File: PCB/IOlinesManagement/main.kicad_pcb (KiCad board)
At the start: 2 copper layers, 177.8 x 104 mm, 286 parts, among them K1 HK19F-DCxxV-SHC, K10 HK19F-DCxxV-SHC, K11 HK19F-DCxxV-SHC, K12 HK19F-DCxxV-SHC, K13 HK19F-DCxxV-SHC, K14 HK19F-DCxxV-SHC, K15 HK19F-DCxxV-SHC, K16 HK19F-DCxxV-SHC, K2 HK19F-DCxxV-SHC, K3 HK19F-DCxxV-SHC, K4 HK19F-DCxxV-SHC, K5 HK19F-DCxxV-SHC, K6 HK19F-DCxxV-SHC, K7 HK19F-DCxxV-SHC, K8 HK19F-DCxxV-SHC, K9 HK19F-DCxxV-SHC, Q1 BC817, Q10 BC817, Q11 BC817, Q12 BC817, Q13 BC817, Q14 BC817, Q15 BC817, Q16 BC817, Q17 BC817, Q18 BC817, Q19 BC817, Q2 BC817, Q20 BC817, Q21 BC817, Q22 BC817, Q23 BC337, Q24 BC337, Q25 BC337, Q26 BC337, Q27 BC337, Q28 BC337, Q29 BC337, Q3 BC817, Q30 BC337, Q31 BC337, Q32 BC337, Q33 BC337, Q34 BC337, Q35 BC327, Q36 BC337, Q37 BC337, Q38 BC337, Q39 BC337, Q4 BC817, Q40 BC337, Q41 BC337, Q42 BC337, Q43 BC337, Q44 BC337, Q45 BC337, Q46 BC337, Q47 BC337, Q48 BC337, Q49 BC337, Q5 BC817, Q50 BC337, Q51 BC327, Q52 BC337, Q53 BC337, Q54 BC337, Q55 BC337, Q56 BC337, Q57 BC337, Q58 BC337, Q59 BC337, Q6 BC817, Q60 BC337, Q61 BC337, Q62 BC337, Q63 BC337, Q64 BC337, Q65 BC337, Q66 BC337, Q67 BC327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

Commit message: 99% completed release
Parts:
- removed ExtPwr_1: Conn_01x02, Connector_PinHeader_2.54mm:PinHeader_2x09_P2.54mm_Vertical
- removed Q65, Q66: BC337, Package_TO_SOT_THT:TO-92_Inline_Wide
- removed Q67, Q68, Q69, Q70, Q71, Q72, Q73, Q74, Q75, Q76, Q77, Q78, Q79, Q80: BC327, Package_TO_SOT_THT:TO-92_Inline_Wide
- removed Q81, Q82, Q83, Q84, Q85, Q86, Q87, Q88, Q89, Q90: BC817, Package_TO_SOT_SMD:SOT-23
- Q17, Q19, Q21: value BC817 -> BC327; footprint Package_TO_SOT_SMD:SOT-23 -> Package_TO_SOT_THT:TO-92_Inline_Wide
- Q18, Q20, Q22: value BC817 -> BC337; footprint Package_TO_SOT_SMD:SOT-23 -> Package_TO_SOT_THT:TO-92_Inline_Wide
- Q23, Q25, Q26, Q28, Q30, Q32, Q34, Q37, Q39, Q41, Q43, Q45, Q47, Q49, Q52, Q53, Q54, Q55, Q56, Q57, Q58, Q59, Q60, Q61, Q62, Q63, Q64: value BC337 -> BC327
- R100, R101, R104, R29, R32, R42, R45, R46, R73, R74, R97: value 100 -> 50
- R102, R103, R23, R26, R35, R43, R44, R59, R68, R71, R72, R75, R91, R94: value 100 -> 5K
- R17, R18, R19, R20, R55, R83: value 10K -> 100K
- R21, R50, R53, R81: value 10K -> 50
- R22, R47, R51, R52, R76, R79, R80: value 10K -> 5K
- R24, R25, R28, R33, R36, R57, R60, R66, R69, R70, R89, R92, R93, R96: value 5K -> 50
- R37, R39, R61, R63, R64, R86, R87: value 5K -> 100K
- R38, R41, R62, R85, R88: value 100 -> 100K
- R40: value 5K -> 10K
- R48: value 1K -> 5K
- R49, R78: value 100K -> 50
- R54, R82: value 10K -> 1K
- R56, R65: value 100 -> 10K
- R77: value 1K -> 50
- moved Q45 339.7 mm to (188.7, 142.8)
- moved Q37 335.9 mm to (188.7, 120.3)
- moved Q29 332.8 mm to (184.3, 81.0)
- moved Q19 331.0 mm to (187.8, 74.8)
- moved Q46 324.3 mm to (183.9, 127.4)
- moved Q63 321.0 mm to (177.1, 126.6), turned to 180 degrees
- moved Q20 318.9 mm to (184.2, 59.2)
- moved Q38 310.1 mm to (183.9, 104.7)
- moved Q26 306.6 mm to (158.2, 96.6)
- moved Q64 304.6 mm to (177.1, 104.1), turned to 180 degrees
- moved R70 303.9 mm to (193.6, 115.1), turned to 90 degrees
- moved Q36 303.0 mm to (154.2, 104.9)
- moved Q18 301.6 mm to (153.8, 58.8)
- moved R93 301.2 mm to (193.6, 137.7), turned to 90 degrees
- moved R86 298.8 mm to (179.3, 127.1), turned to -90 degrees
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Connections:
- K10 pad A1: Net-(Q10-C) -> Net-(Q11-C)
- K11 pad A1: Net-(Q11-C) -> Net-(Q12-C)
- K12 pad A1: Net-(Q12-C) -> Net-(Q9-C)
- K13 pad A1: Net-(Q16-C) -> Net-(Q14-C)
- K14 pad A1: Net-(Q15-C) -> Net-(Q13-C)
- K15 pad A1: Net-(Q14-C) -> Net-(Q15-C)
- K16 pad A1: Net-(Q13-C) -> Net-(Q16-C)
- K5 pad A1: Net-(Q5-C) -> Net-(Q7-C)
- K7 pad A1: Net-(Q7-C) -> Net-(Q8-C)
- K8 pad A1: Net-(Q8-C) -> Net-(Q5-C)
- K9 pad A1: Net-(Q9-C) -> Net-(Q10-C)
- Q17 pad 1: Net-(Q17-B) -> OutputToDev_9
- Q17 pad 2: GND -> Net-(Q17-B)
- Q17 pad 3: Net-(Q17-C) -> Net-(Q17-E)
- Q18 pad 1: Net-(Q18-B) -> OutputToDev_9
- Q18 pad 2: GND -> Net-(Q18-B)
- Q18 pad 3: Net-(Q18-C) -> Net-(Q18-E)
- Q19 pad 1: Net-(Q19-B) -> OutputToDev_13
- Q19 pad 2: GND -> Net-(Q19-B)
- Q19 pad 3: Net-(Q19-C) -> Net-(Q19-E)
- Q20 pad 1: Net-(Q20-B) -> OutputToDev_13
- Q20 pad 2: GND -> Net-(Q20-B)
- Q20 pad 3: Net-(Q20-C) -> Net-(Q20-E)
- Q21 pad 1: Net-(Q21-B) -> OutputToDev_1
- Q21 pad 2: GND -> Net-(Q21-B)
- Q21 pad 3: Net-(Q21-C) -> Net-(Q21-E)
- Q22 pad 1: Net-(Q22-B) -> OutputToDev_1
- Q22 pad 2: GND -> Net-(Q22-B)
- Q22 pad 3: Net-(Q22-C) -> Net-(Q22-E)
- Q23 pad 1: Net-(Q23-C) -> OutputToDev_5
- Q23 pad 3: OutputToDev_1 -> Net-(Q23-E)
- Q24 pad 1: Net-(Q24-C) -> OutputToDev_5
- Q24 pad 2: Net-(Q17-C) -> Net-(Q24-B)
- Q24 pad 3: GND -> Net-(Q24-E)
- Q25 pad 1: Net-(Q25-C) -> InputToMC_1
- Q25 pad 3: OutputToDev_4 -> Net-(Q25-E)
- Q26 pad 1: Net-(Q26-C) -> OutputToDev_10
- Q26 pad 3: GND -> Net-(Q26-E)
- Q27 pad 1: Net-(Q27-C) -> OutputToDev_10
- Q27 pad 3: OutputToDev_7 -> Net-(Q27-E)
- Q28 pad 1: Net-(Q28-C) -> OutputToDev_14
- Q28 pad 2: Net-(Q18-C) -> Net-(Q28-B)
- Q28 pad 3: GND -> Net-(Q28-E)
- Q29 pad 1: Net-(Q29-C) -> OutputToDev_14
- Q29 pad 3: OutputToDev_13 -> Net-(Q29-E)
- Q30 pad 1: Net-(Q30-C) -> OutputToDev_2
- Q30 pad 3: GND -> Net-(Q30-E)
- Q31 pad 1: Net-(Q31-C) -> OutputToDev_2
- Q31 pad 3: OutputToDev_10 -> Net-(Q31-E)
- Q32 pad 1: Net-(Q32-C) -> OutputToDev_6
- Q32 pad 2: Net-(Q19-C) -> Net-(Q32-B)
- Q32 pad 3: GND -> Net-(Q32-E)
- Q33 pad 1: Net-(Q33-C) -> OutputToDev_6
- Q33 pad 3: OutputToDev_16 -> Net-(Q33-E)
- Q34 pad 1: Net-(Q34-C) -> InputToMC_2
- Q34 pad 3: GND -> Net-(Q34-E)
- Q35 pad 1: InputToMC_1 -> OutputToDev_11
- Q36 pad 1: Net-(Q36-C) -> OutputToDev_11
- Q36 pad 3: GND -> Net-(Q36-E)
- Q37 pad 1: Net-(Q37-C) -> OutputToDev_15
- Q37 pad 3: GND -> Net-(Q37-E)
- Q38 pad 1: Net-(Q38-C) -> OutputToDev_15
- Q38 pad 3: GND -> Net-(Q38-E)
- Q39 pad 1: Net-(Q39-C) -> OutputToDev_3
- Q39 pad 3: unconnected-(Q39-E-Pad3) -> Net-(Q39-E)
- Q40 pad 1: Net-(Q40-C) -> OutputToDev_3
- Q40 pad 3: GND -> Net-(Q40-E)
- Q41 pad 1: Net-(Q41-C) -> OutputToDev_7
- Q41 pad 3: OutputToDev_2 -> Net-(Q41-E)
- Q42 pad 1: Net-(Q42-C) -> OutputToDev_7
- Q42 pad 3: GND -> Net-(Q42-E)
- Q43 pad 1: Net-(Q43-C) -> OutputToDev_12
- Q43 pad 3: OutputToDev_5 -> Net-(Q43-E)
- Q44 pad 1: Net-(Q44-C) -> OutputToDev_12
- Q44 pad 3: GND -> Net-(Q44-E)
- Q45 pad 1: Net-(Q45-C) -> OutputToDev_16
- Q45 pad 3: OutputToDev_8 -> Net-(Q45-E)
- Q46 pad 1: Net-(Q46-C) -> OutputToDev_16
- Q46 pad 2: Net-(Q22-C) -> Net-(Q46-B)
- Q46 pad 3: GND -> Net-(Q46-E)
- Q47 pad 1: Net-(Q47-C) -> OutputToDev_4
- Q47 pad 3: OutputToDev_14 -> Net-(Q47-E)
- Q48 pad 1: Net-(Q48-C) -> OutputToDev_4
- Q48 pad 2: Net-(Q20-C) -> Net-(Q48-B)
- Q48 pad 3: GND -> Net-(Q48-E)
- Q49 pad 1: Net-(Q49-C) -> OutputToDev_8
- Q49 pad 3: OutputToDev_11 -> Net-(Q49-E)
- Q50 pad 1: Net-(Q50-C) -> OutputToDev_8
- Q50 pad 2: Net-(Q21-C) -> Net-(Q50-B)
- Q50 pad 3: GND -> Net-(Q50-E)
- Q51 pad 1: InputToMC_2 -> InputToMC_8
- Q52 pad 1: Net-(Q52-C) -> InputToMC_10
- Q52 pad 3: GND -> Net-(Q52-E)
- Q53 pad 1: Net-(Q53-C) -> InputToMC_5
- Q53 pad 3: GND -> Net-(Q53-E)
- Q54 pad 1: Net-(Q54-C) -> InputToMC_9
- Q54 pad 3: GND -> Net-(Q54-E)
- Q55 pad 1: Net-(Q55-C) -> InputToMC_12
- Q55 pad 3: GND -> Net-(Q55-E)
- Q56 pad 1: Net-(Q56-C) -> InputToMC_11
- Q56 pad 3: GND -> Net-(Q56-E)
- Q57 pad 1: Net-(Q57-C) -> InputToMC_4
- Q57 pad 3: OutputToDev_3 -> Net-(Q57-E)
- Q58 pad 1: Net-(Q58-C) -> InputToMC_3
- Q58 pad 3: GND -> Net-(Q58-E)
- Q59 pad 1: Net-(Q59-C) -> InputToMC_6
- Q59 pad 3: OutputToDev_6 -> Net-(Q59-E)
- Q60 pad 1: Net-(Q60-C) -> InputToMC_14
- Q60 pad 3: GND -> Net-(Q60-E)
- Q61 pad 1: Net-(Q61-C) -> InputToMC_7
- Q61 pad 3: OutputToDev_9 -> Net-(Q61-E)
- Q62 pad 1: Net-(Q62-C) -> InputToMC_13
- Q62 pad 3: GND -> Net-(Q62-E)
- Q63 pad 1: Net-(Q63-C) -> InputToMC_16
- Q63 pad 3: OutputToDev_15 -> Net-(Q63-E)
- Q64 pad 1: Net-(Q64-C) -> InputToMC_15
- Q64 pad 3: GND -> Net-(Q64-E)
- R10 pad 1: Net-(Q10-B) -> Net-(Q11-B)
- R100 pad 1: OutputToDev_3 -> Net-(Q48-E)
- R100 pad 2: Net-(Q58-C) -> GND
- R101 pad 1: OutputToDev_6 -> Net-(Q49-E)
- R101 pad 2: Net-(Q60-C) -> +5V
- R102 pad 1: OutputToDev_9 -> OutputToMC_8
- R102 pad 2: Net-(Q62-C) -> Net-(Q49-B)
- R103 pad 1: OutputToDev_15 -> OutputToMC_8
- R103 pad 2: Net-(Q64-C) -> Net-(Q50-B)
- R104 pad 1: OutputToDev_12 -> Net-(Q50-E)
- R104 pad 2: Net-(Q66-C) -> GND
- R11 pad 1: Net-(Q9-B) -> Net-(Q10-B)
- R112 pad 1: Net-(Q67-E) -> Net-(Q51-E)
- R113 pad 1: Net-(Q68-E) -> Net-(Q52-E)
- R114 pad 1: Net-(Q69-E) -> Net-(Q53-E)
- R115 pad 1: Net-(Q67-B) -> Net-(Q51-B)
- R116 pad 2: Net-(Q67-B) -> Net-(Q51-B)
- R117 pad 1: Net-(Q70-E) -> Net-(Q54-E)
- R118 pad 1: Net-(Q68-B) -> Net-(Q52-B)
- R119 pad 2: Net-(Q68-B) -> Net-(Q52-B)
- R12 pad 1: Net-(Q11-B) -> Net-(Q12-B)
- R120 pad 1: Net-(Q71-E) -> Net-(Q55-E)
- R121 pad 1: Net-(Q69-B) -> Net-(Q53-B)
- R122 pad 2: Net-(Q69-B) -> Net-(Q53-B)
- R123 pad 1: Net-(Q70-B) -> Net-(Q54-B)
- R124 pad 2: Net-(Q70-B) -> Net-(Q54-B)
- R125 pad 1: Net-(Q72-E) -> Net-(Q56-E)
- R126 pad 1: Net-(Q71-B) -> Net-(Q55-B)
- R127 pad 2: Net-(Q71-B) -> Net-(Q55-B)
- R128 pad 1: Net-(Q73-E) -> Net-(Q57-E)
- R129 pad 1: Net-(Q72-B) -> Net-(Q56-B)
- R13 pad 1: Net-(Q16-B) -> Net-(Q14-B)
- R130 pad 2: Net-(Q72-B) -> Net-(Q56-B)
- R131 pad 1: Net-(Q73-B) -> Net-(Q57-B)
- R132 pad 2: Net-(Q73-B) -> Net-(Q57-B)
- R14 pad 1: Net-(Q14-B) -> Net-(Q15-B)
- R140 pad 1: Net-(Q74-E) -> Net-(Q58-E)
- R141 pad 1: Net-(Q74-B) -> Net-(Q58-B)
- R142 pad 2: Net-(Q74-B) -> Net-(Q58-B)
- R143 pad 1: Net-(Q75-E) -> Net-(Q59-E)
- R144 pad 1: Net-(Q75-B) -> Net-(Q59-B)
- R145 pad 2: Net-(Q75-B) -> Net-(Q59-B)
- R146 pad 1: Net-(Q76-E) -> Net-(Q60-E)
- R147 pad 1: Net-(Q77-E) -> Net-(Q61-E)
- R148 pad 1: Net-(Q78-E) -> Net-(Q62-E)
- R149 pad 1: Net-(Q76-B) -> Net-(Q60-B)
- R15 pad 1: Net-(Q13-B) -> Net-(Q16-B)
- R150 pad 2: Net-(Q76-B) -> Net-(Q60-B)
- R151 pad 1: Net-(Q79-E) -> Net-(Q63-E)
- R152 pad 1: Net-(Q77-B) -> Net-(Q61-B)
- R153 pad 2: Net-(Q77-B) -> Net-(Q61-B)
- R154 pad 1: Net-(Q78-B) -> Net-(Q62-B)
- R155 pad 2: Net-(Q78-B) -> Net-(Q62-B)
- R156 pad 1: Net-(Q80-E) -> Net-(Q64-E)
- R157 pad 1: Net-(Q79-B) -> Net-(Q63-B)
- R158 pad 2: Net-(Q79-B) -> Net-(Q63-B)
- R159 pad 1: Net-(Q80-B) -> Net-(Q64-B)
- R16 pad 1: Net-(Q15-B) -> Net-(Q13-B)
- R160 pad 2: Net-(Q80-B) -> Net-(Q64-B)
- R17 pad 1: OutputToMC_1 -> GND
- R17 pad 2: Net-(Q17-B) -> OutputToDev_9
- R18 pad 1: OutputToMC_4 -> GND
- R18 pad 2: Net-(Q81-B) -> OutputToDev_13
- R19 pad 1: OutputToMC_7 -> GND
- R19 pad 2: Net-(Q18-B) -> OutputToDev_1
- R20 pad 1: OutputToMC_13 -> GND
- R20 pad 2: Net-(Q82-B) -> OutputToDev_5
- R21 pad 1: OutputToMC_10 -> Net-(Q17-E)
- R21 pad 2: Net-(Q19-B) -> +5V
- R22 pad 1: OutputToMC_16 -> OutputToMC_9
- R22 pad 2: Net-(Q83-B) -> Net-(Q17-B)
- R23 pad 1: VCC -> OutputToMC_9
- R23 pad 2: Net-(Q23-C) -> Net-(Q18-B)
- R24 pad 1: Net-(Q23-B) -> Net-(Q18-E)
- R24 pad 2: OutputToMC_1 -> GND
- R25 pad 1: +5V -> Net-(Q19-E)
- R25 pad 2: Net-(Q17-C) -> +5V
- R26 pad 1: VCC -> OutputToMC_13
- R26 pad 2: Net-(Q25-C) -> Net-(Q19-B)
- R27 pad 1: Net-(Q25-B) -> OutputToMC_13
- R27 pad 2: OutputToMC_4 -> Net-(Q20-B)
- R28 pad 1: +5V -> Net-(Q21-E)
- R28 pad 2: Net-(Q26-B) -> +5V
- R29 pad 1: VCC -> Net-(Q20-E)
- R29 pad 2: Net-(Q27-C) -> GND
- R30 pad 1: Net-(Q27-B) -> OutputToMC_1
- R30 pad 2: OutputToMC_7 -> Net-(Q21-B)
- R31 pad 1: +5V -> OutputToMC_1
- R31 pad 2: Net-(Q18-C) -> Net-(Q22-B)
- R32 pad 1: VCC -> Net-(Q22-E)
- R32 pad 2: Net-(Q29-C) -> GND
- R33 pad 1: Net-(Q29-B) -> Net-(Q23-E)
- R33 pad 2: OutputToMC_13 -> +5V
- R34 pad 1: +5V -> OutputToMC_5
- R34 pad 2: Net-(Q30-B) -> Net-(Q23-B)
- R35 pad 1: VCC -> OutputToMC_5
- R35 pad 2: Net-(Q31-C) -> Net-(Q24-B)
- R36 pad 1: Net-(Q31-B) -> Net-(Q24-E)
- R36 pad 2: OutputToMC_10 -> GND
- R37 pad 1: +5V -> GND
- R37 pad 2: Net-(Q19-C) -> OutputToDev_10
- R38 pad 1: VCC -> GND
- R38 pad 2: Net-(Q33-C) -> OutputToDev_14
- R39 pad 1: Net-(Q33-B) -> GND
- R39 pad 2: OutputToMC_16 -> OutputToDev_2
- R40 pad 1: +5V -> InputToMC_1
- R40 pad 2: Net-(Q34-B) -> GND
- R41 pad 1: OutputToDev_1 -> GND
- R41 pad 2: Net-(Q24-C) -> OutputToDev_6
- R42 pad 1: OutputToDev_4 -> Net-(Q26-E)
- R42 pad 2: Net-(Q26-C) -> +5V
- R43 pad 1: OutputToDev_7 -> OutputToMC_10
- R43 pad 2: Net-(Q28-C) -> Net-(Q26-B)
- R44 pad 1: OutputToDev_13 -> OutputToMC_10
- R44 pad 2: Net-(Q30-C) -> Net-(Q27-B)
- R45 pad 1: OutputToDev_10 -> Net-(Q27-E)
- R45 pad 2: Net-(Q32-C) -> GND
- R46 pad 1: OutputToDev_16 -> Net-(Q28-E)
- R46 pad 2: Net-(Q34-C) -> +5V
- R47 pad 1: InputToMC_1 -> OutputToMC_14
- R47 pad 2: GND -> Net-(Q28-B)
- R48 pad 1: Net-(Q35-E) -> OutputToMC_14
- R48 pad 2: +5V -> Net-(Q29-B)
- R49 pad 1: Net-(Q35-B) -> Net-(Q30-E)
- R5 pad 1: Net-(Q5-B) -> Net-(Q7-B)
- R50 pad 1: InputToDev_1 -> Net-(Q29-E)
- R50 pad 2: Net-(Q35-B) -> GND
- R51 pad 2: Net-(Q85-B) -> Net-(Q30-B)
- R52 pad 1: OutputToMC_5 -> OutputToMC_2
- R52 pad 2: Net-(Q84-B) -> Net-(Q31-B)
- R53 pad 1: OutputToMC_8 -> Net-(Q31-E)
- R53 pad 2: Net-(Q22-B) -> GND
- R54 pad 1: OutputToMC_14 -> Net-(Q25-E)
- R54 pad 2: Net-(Q20-B) -> +5V
- R55 pad 1: OutputToMC_11 -> Net-(Q25-B)
- R55 pad 2: Net-(Q21-B) -> +5V
- R56 pad 1: VCC -> InputToDev_1
- R56 pad 2: Net-(Q41-C) -> Net-(Q25-B)
- R57 pad 1: Net-(Q41-B) -> Net-(Q32-E)
- R57 pad 2: OutputToMC_2 -> +5V
- R58 pad 1: +5V -> OutputToMC_6
- R58 pad 2: Net-(Q42-B) -> Net-(Q32-B)
- R59 pad 1: VCC -> OutputToMC_6
- R59 pad 2: Net-(Q43-C) -> Net-(Q33-B)
- R6 pad 1: Net-(Q7-B) -> Net-(Q8-B)
- R60 pad 1: Net-(Q43-B) -> Net-(Q33-E)
- R60 pad 2: OutputToMC_5 -> GND
- R61 pad 1: +5V -> GND
- R61 pad 2: Net-(Q44-B) -> OutputToDev_11
- R62 pad 1: VCC -> GND
- R62 pad 2: Net-(Q45-C) -> OutputToDev_15
- R63 pad 1: Net-(Q45-B) -> GND
- R63 pad 2: OutputToMC_8 -> OutputToDev_3
- R64 pad 1: +5V -> GND
- R64 pad 2: Net-(Q22-C) -> OutputToDev_7
- R65 pad 1: VCC -> InputToMC_2
- R65 pad 2: Net-(Q47-C) -> GND
- R66 pad 1: Net-(Q47-B) -> Net-(Q35-E)
- R66 pad 2: OutputToMC_14 -> +5V
- R67 pad 1: +5V -> OutputToMC_11
- R67 pad 2: Net-(Q20-C) -> Net-(Q35-B)
- R68 pad 1: VCC -> OutputToMC_11
- R68 pad 2: Net-(Q49-C) -> Net-(Q36-B)
- R69 pad 1: Net-(Q49-B) -> Net-(Q36-E)
- R69 pad 2: OutputToMC_11 -> GND
- R7 pad 1: Net-(Q8-B) -> Net-(Q5-B)
- R70 pad 1: +5V -> Net-(Q37-E)
- R70 pad 2: Net-(Q21-C) -> +5V
- R71 pad 1: OutputToDev_2 -> OutputToMC_15
- R71 pad 2: Net-(Q42-C) -> Net-(Q37-B)
- R72 pad 1: OutputToDev_5 -> OutputToMC_15
- R72 pad 2: Net-(Q44-C) -> Net-(Q38-B)
- R73 pad 1: OutputToDev_8 -> Net-(Q39-E)
- R73 pad 2: Net-(Q46-C) -> +5V
- R74 pad 1: OutputToDev_14 -> Net-(Q38-E)
- R74 pad 2: Net-(Q48-C) -> GND
- R75 pad 1: OutputToDev_11 -> OutputToMC_3
- R75 pad 2: Net-(Q50-C) -> Net-(Q39-B)
- R76 pad 1: InputToMC_2 -> OutputToMC_3
- R76 pad 2: GND -> Net-(Q40-B)
- R77 pad 1: Net-(Q51-E) -> Net-(Q40-E)
- R77 pad 2: +5V -> GND
- R78 pad 1: Net-(Q51-B) -> Net-(Q41-E)
- R79 pad 1: InputToDev_2 -> OutputToMC_7
- R79 pad 2: Net-(Q51-B) -> Net-(Q41-B)
- R80 pad 1: OutputToMC_3 -> OutputToMC_7
- R80 pad 2: Net-(Q86-B) -> Net-(Q42-B)
- R81 pad 1: OutputToMC_6 -> Net-(Q42-E)
- R81 pad 2: Net-(Q87-B) -> GND
- R82 pad 1: OutputToMC_9 -> Net-(Q34-E)
- R82 pad 2: Net-(Q88-B) -> +5V
- R83 pad 1: OutputToMC_15 -> Net-(Q34-B)
- R83 pad 2: Net-(Q90-B) -> +5V
- R84 pad 1: OutputToMC_12 -> InputToDev_2
- R84 pad 2: Net-(Q89-B) -> Net-(Q34-B)
- R85 pad 1: VCC -> GND
- R85 pad 2: Net-(Q57-C) -> OutputToDev_12
- R86 pad 1: Net-(Q57-B) -> GND
- R86 pad 2: OutputToMC_3 -> OutputToDev_16
- R87 pad 1: +5V -> GND
- R87 pad 2: Net-(Q58-B) -> OutputToDev_4
- R88 pad 1: VCC -> GND
- R88 pad 2: Net-(Q59-C) -> OutputToDev_8
- R89 pad 1: Net-(Q59-B) -> Net-(Q43-E)
- R89 pad 2: OutputToMC_6 -> +5V
- R9 pad 2: Net-(Q12-B) -> Net-(Q9-B)
- R90 pad 1: +5V -> OutputToMC_12
- R90 pad 2: Net-(Q60-B) -> Net-(Q43-B)
- R91 pad 1: VCC -> OutputToMC_12
- R91 pad 2: Net-(Q61-C) -> Net-(Q44-B)
- R92 pad 1: Net-(Q61-B) -> Net-(Q44-E)
- R92 pad 2: OutputToMC_9 -> GND
- R93 pad 1: +5V -> Net-(Q45-E)
- R93 pad 2: Net-(Q62-B) -> +5V
- R94 pad 1: VCC -> OutputToMC_16
- R94 pad 2: Net-(Q63-C) -> Net-(Q45-B)
- R95 pad 1: Net-(Q63-B) -> OutputToMC_16
- R95 pad 2: OutputToMC_15 -> Net-(Q46-B)
- R96 pad 1: +5V -> Net-(Q47-E)
- R96 pad 2: Net-(Q64-B) -> +5V
- R97 pad 1: VCC -> Net-(Q46-E)
- R97 pad 2: Net-(Q65-C) -> GND
- R98 pad 1: Net-(Q65-B) -> OutputToMC_4
- R98 pad 2: OutputToMC_12 -> Net-(Q47-B)
- R99 pad 1: +5V -> OutputToMC_4
- R99 pad 2: Net-(Q66-B) -> Net-(Q48-B)
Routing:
- net GND: track 44.5 -> 1097.6 mm, vias 3 -> 64
- net +5V: track 112.7 -> 850.5 mm, vias 6 -> 3
- net DIR-4: track 58.7 -> 0.00 mm
- net DIR-3: track 36.7 -> 0.00 mm
- net DIR-1: track 29.9 -> 0.00 mm, vias 1 -> 0
- net InputToMC_9: track 0.00 -> 29.0 mm, vias 0 -> 1
- net InputToMC_13: track 0.00 -> 27.7 mm, vias 0 -> 1
- net InputToMC_6: track 0.00 -> 27.6 mm, vias 0 -> 1
- net InputToMC_3: track 0.00 -> 27.5 mm, vias 0 -> 1
- net InputToMC_10: track 0.00 -> 27.5 mm, vias 0 -> 1
- net InputToMC_4: track 0.00 -> 27.4 mm, vias 0 -> 1
- net InputToMC_15: track 0.00 -> 27.3 mm, vias 0 -> 1
- net InputToMC_7: track 0.00 -> 27.2 mm, vias 0 -> 1
- net InputToMC_14: track 0.00 -> 27.2 mm, vias 0 -> 1
- net InputToMC_16: track 0.00 -> 27.2 mm, vias 0 -> 1
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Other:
- board size 177.8 x 104 mm -> 156 x 93.6 mm

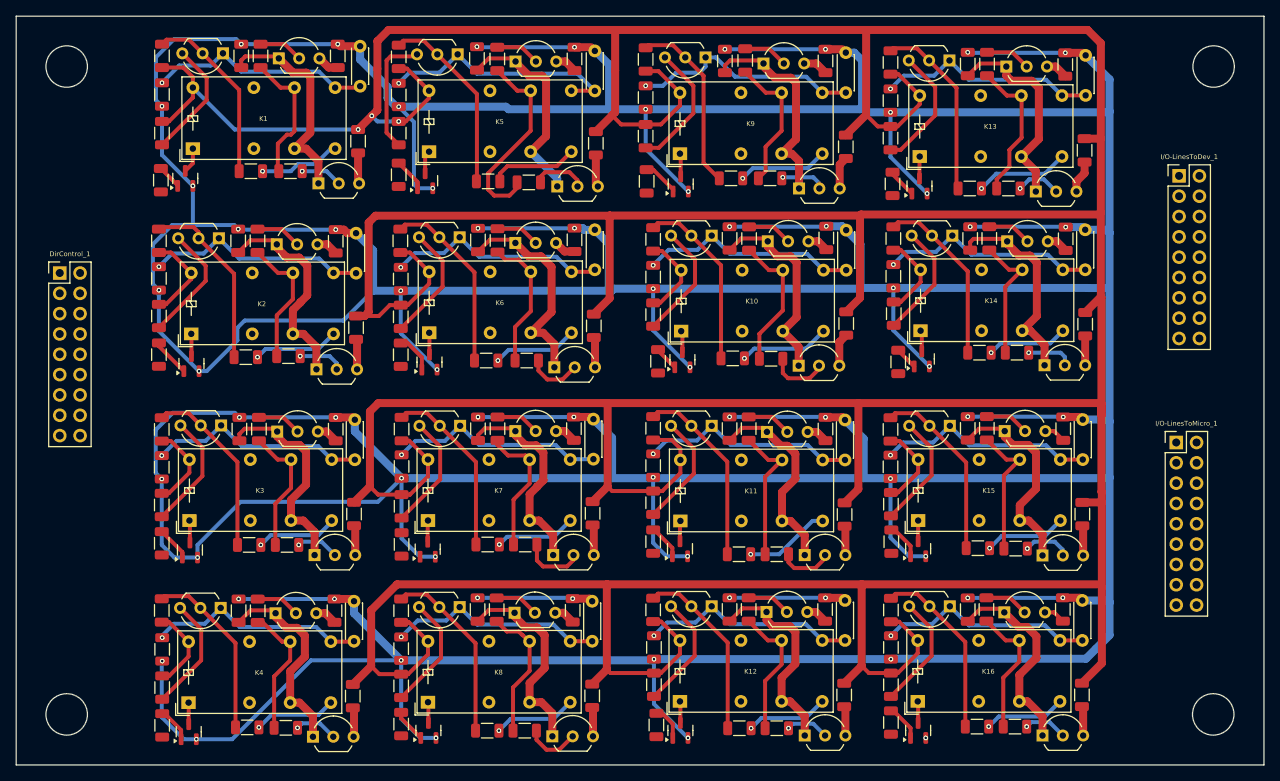
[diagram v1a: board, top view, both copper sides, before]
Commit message: First completed release
In order to avoid the size explosion, I have been forced to use a multilayer PCB.
It increases the building prices, I know it.
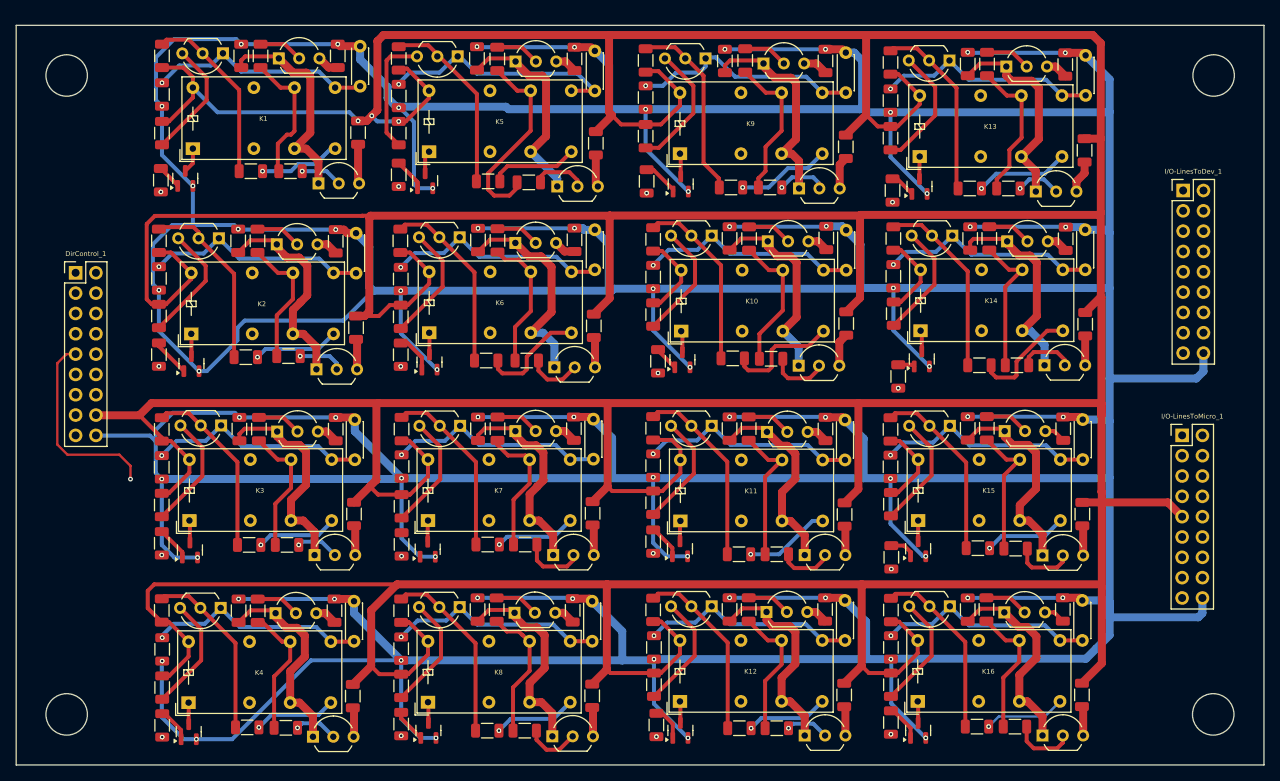
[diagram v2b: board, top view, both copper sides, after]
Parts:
- moved DirControl_1 1.98 mm to (67.8, 85.0)
- moved R14 1.96 mm to (169.8, 120.5)
- moved I/O-LinesToDev_1 1.90 mm to (206.2, 74.7)
- moved R16 1.81 mm to (170.6, 97.9)
- moved R150 1.57 mm to (180.8, 96.5)
- moved R47 1.57 mm to (185.5, 96.5)
- moved I/O-LinesToMicro_1 1.15 mm to (206.1, 105.3)
- moved R124 1.14 mm to (149.7, 74.3)
- moved R22 1.14 mm to (154.6, 74.3)
- moved R28 1.08 mm to (103.1, 67.4)
- moved R13 0.83 mm to (169.9, 74.7)
- moved Q53 0.25 mm to (115.6, 57.9)
- moved R121 0.19 mm to (108.2, 58.2)
- moved R107 0.13 mm to (108.2, 62.9)
- moved R123 0.13 mm to (139.1, 58.4)
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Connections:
- DirControl_1 pad 1: DIR-6 -> DIR-13
- DirControl_1 pad 10: DIR-9 -> DIR-3
- DirControl_1 pad 11: DIR-10 -> DIR-16
- DirControl_1 pad 12: DIR-11 -> DIR-7
- DirControl_1 pad 14: DIR-13 -> DIR-11
- DirControl_1 pad 15: DIR-14 -> DIR-8
- DirControl_1 pad 16: DIR-15 -> +5V
- DirControl_1 pad 17: DIR-16 -> DIR-4
- DirControl_1 pad 2: DIR-1 -> DIR-2
- DirControl_1 pad 3: DIR-7 -> DIR-9
- DirControl_1 pad 4: DIR-2 -> DIR-6
- DirControl_1 pad 6: DIR-3 -> DIR-10
- DirControl_1 pad 7: DIR-8 -> DIR-1
- DirControl_1 pad 8: DIR-4 -> DIR-14
- DirControl_1 pad 9: +5V -> DIR-15
- I/O-LinesToDev_1 pad 1: I/O-1 Port -> I/O-2 Port
- I/O-LinesToDev_1 pad 10: I/O-9 Port -> unconnected-(I/O-LinesToDev_1-Pin_10-Pad10)
- I/O-LinesToDev_1 pad 11: I/O-10 Port -> I/O-15 Port
- I/O-LinesToDev_1 pad 12: I/O-11 Port -> I/O-16 Port
- I/O-LinesToDev_1 pad 13: I/O-12 Port -> I/O-11 Port
- I/O-LinesToDev_1 pad 14: I/O-13 Port -> I/O-12 Port
- I/O-LinesToDev_1 pad 15: I/O-14 Port -> I/O-7 Port
- I/O-LinesToDev_1 pad 16: I/O-15 Port -> I/O-8 Port
- I/O-LinesToDev_1 pad 17: I/O-16 Port -> I/O-4 Port
- I/O-LinesToDev_1 pad 18: unconnected-(I/O-LinesToDev_1-Pin_18-Pad18) -> GND
- I/O-LinesToDev_1 pad 2: I/O-2 Port -> I/O-13 Port
- I/O-LinesToDev_1 pad 3: I/O-3 Port -> I/O-6 Port
- I/O-LinesToDev_1 pad 4: I/O-4 Port -> I/O-5 Port
- I/O-LinesToDev_1 pad 5: I/O-5 Port -> I/O-10 Port
- I/O-LinesToDev_1 pad 6: I/O-6 Port -> I/O-9 Port
- I/O-LinesToDev_1 pad 7: I/O-7 Port -> I/O-14 Port
- I/O-LinesToDev_1 pad 8: I/O-8 Port -> I/O-1 Port
- I/O-LinesToDev_1 pad 9: unconnected-(I/O-LinesToDev_1-Pin_9-Pad9) -> I/O-3 Port
- I/O-LinesToMicro_1 pad 1: I/O-1 Micro -> I/O-14 Micro
- I/O-LinesToMicro_1 pad 10: I/O-9 Micro -> I/O-4 Micro
- I/O-LinesToMicro_1 pad 11: I/O-10 Micro -> I/O-15 Micro
- I/O-LinesToMicro_1 pad 12: I/O-11 Micro -> I/O-8 Micro
- I/O-LinesToMicro_1 pad 13: I/O-12 Micro -> I/O-11 Micro
- I/O-LinesToMicro_1 pad 14: I/O-13 Micro -> I/O-12 Micro
- I/O-LinesToMicro_1 pad 15: I/O-14 Micro -> I/O-7 Micro
- I/O-LinesToMicro_1 pad 16: I/O-15 Micro -> I/O-16 Micro
- I/O-LinesToMicro_1 pad 17: I/O-16 Micro -> I/O-3 Micro
- I/O-LinesToMicro_1 pad 18: unconnected-(I/O-LinesToMicro_1-Pin_18-Pad18) -> GND
- I/O-LinesToMicro_1 pad 2: I/O-2 Micro -> I/O-1 Micro
- I/O-LinesToMicro_1 pad 3: I/O-3 Micro -> I/O-10 Micro
- I/O-LinesToMicro_1 pad 4: I/O-4 Micro -> I/O-5 Micro
- I/O-LinesToMicro_1 pad 5: I/O-5 Micro -> I/O-6 Micro
- I/O-LinesToMicro_1 pad 6: I/O-6 Micro -> I/O-9 Micro
- I/O-LinesToMicro_1 pad 7: I/O-7 Micro -> I/O-2 Micro
- I/O-LinesToMicro_1 pad 8: I/O-8 Micro -> I/O-13 Micro
- I/O-LinesToMicro_1 pad 9: unconnected-(I/O-LinesToMicro_1-Pin_9-Pad9) -> +5V
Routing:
- net I/O-1 Micro: track 0.00 -> 167.0 mm
- net I/O-4 Port: track 0.00 -> 151.4 mm
- net DIR-16: track 0.00 -> 147.9 mm, vias 0 -> 1
- net I/O-1 Port: track 0.00 -> 145.2 mm
- net I/O-5 Micro: track 0.00 -> 141.0 mm
- net I/O-4 Micro: track 0.00 -> 140.3 mm
- net I/O-3 Port: track 0.00 -> 138.2 mm
- net I/O-8 Port: track 0.00 -> 137.0 mm
- net I/O-2 Micro: track 0.00 -> 135.3 mm
- net DIR-15: track 0.00 -> 131.1 mm, vias 0 -> 2
- net I/O-3 Micro: track 0.00 -> 125.0 mm
- net +5V: track 850.5 -> 975.1 mm
- net I/O-2 Port: track 0.00 -> 123.8 mm
- net I/O-7 Port: track 0.00 -> 116.5 mm
- net DIR-12: track 0.00 -> 114.1 mm, vias 0 -> 1
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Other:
- board size 156 x 93.6 mm -> 156 x 92.4 mm
- copper layers 2 -> 4

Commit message: Small size reduction ans fixes
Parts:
- moved I/O-LinesToDev_1 1.07 mm to (205.2, 74.6)
- moved I/O-LinesToMicro_1 0.94 mm to (205.2, 105.3)
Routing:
- net +5V: track 975.1 -> 988.5 mm
- net I/O-16 Port: track 86.7 -> 80.7 mm
- net I/O-13 Micro: track 85.1 -> 79.7 mm
- net I/O-1 Micro: track 167.0 -> 161.7 mm
- net I/O-12 Port: track 110.1 -> 104.9 mm
- net I/O-5 Micro: track 141.0 -> 135.9 mm
- net I/O-9 Micro: track 112.5 -> 107.6 mm
- net I/O-8 Port: track 137.0 -> 132.0 mm
- net Net-(Q8-B): track 0.00 -> 3.96 mm
- net I/O-13 Port: track 35.6 -> 31.8 mm
- net GND: track 1162.8 -> 1159.9 mm
- net I/O-6 Micro: track 103.5 -> 105.6 mm
- net I/O-4 Micro: track 140.3 -> 142.0 mm
- net I/O-9 Port: track 76.5 -> 74.9 mm
- net I/O-5 Port: track 104.5 -> 102.9 mm
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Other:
- board size 156 x 92.4 mm -> 150.7 x 92.4 mm
